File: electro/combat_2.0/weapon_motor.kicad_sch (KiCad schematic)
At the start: 16 parts, among them J4 Screw_Terminal_01x02, Q1 AO4402G, Q2 AO4402G, Q3 AO4402G, Q4 AO4402G, U4 LM2902, U5 ACS712xLCTR-20A

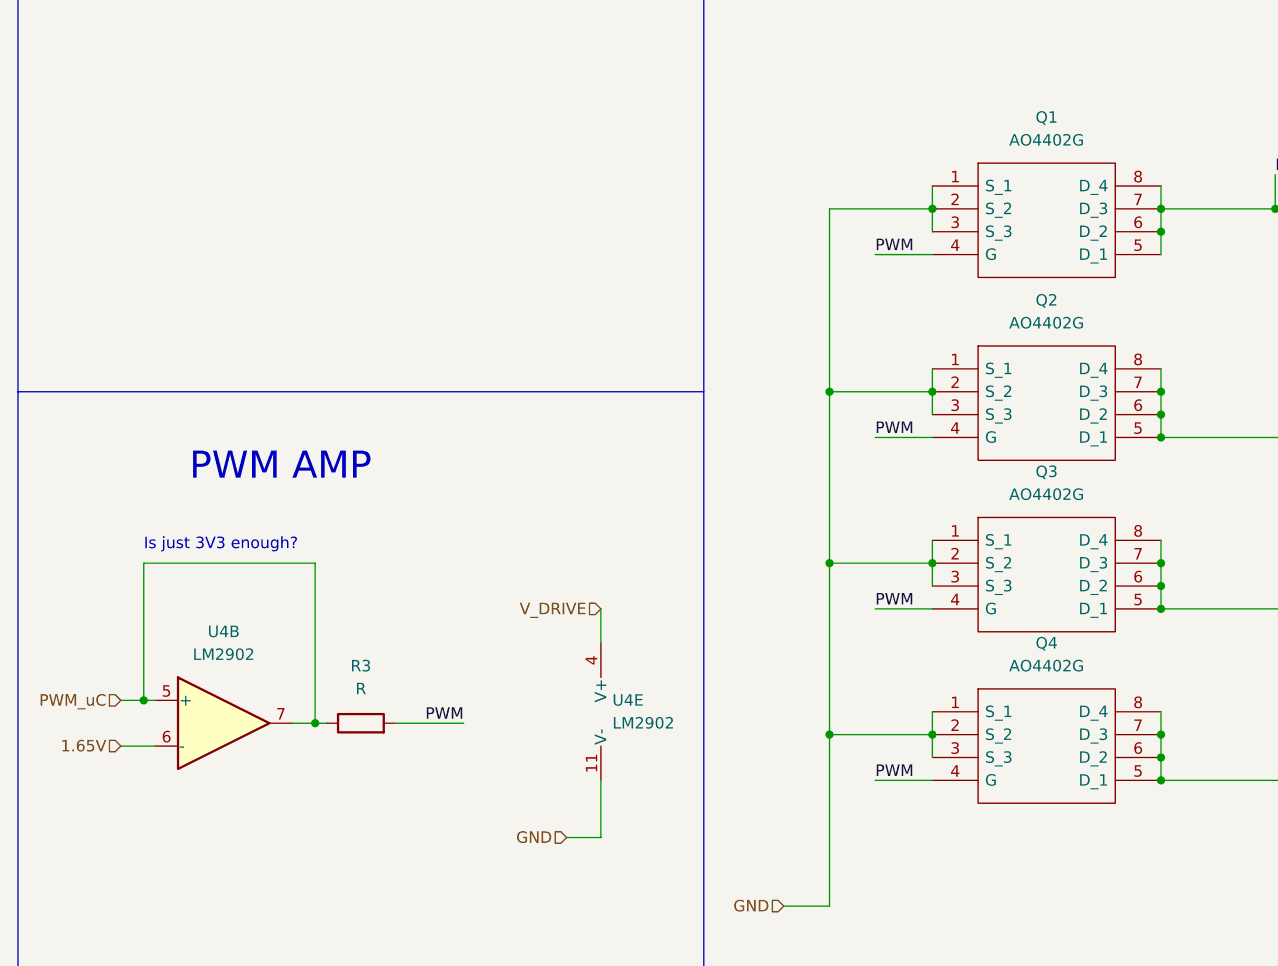
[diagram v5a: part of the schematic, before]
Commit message: Changed MCU to ESP32-DEVKITC, cleared some ERC errors
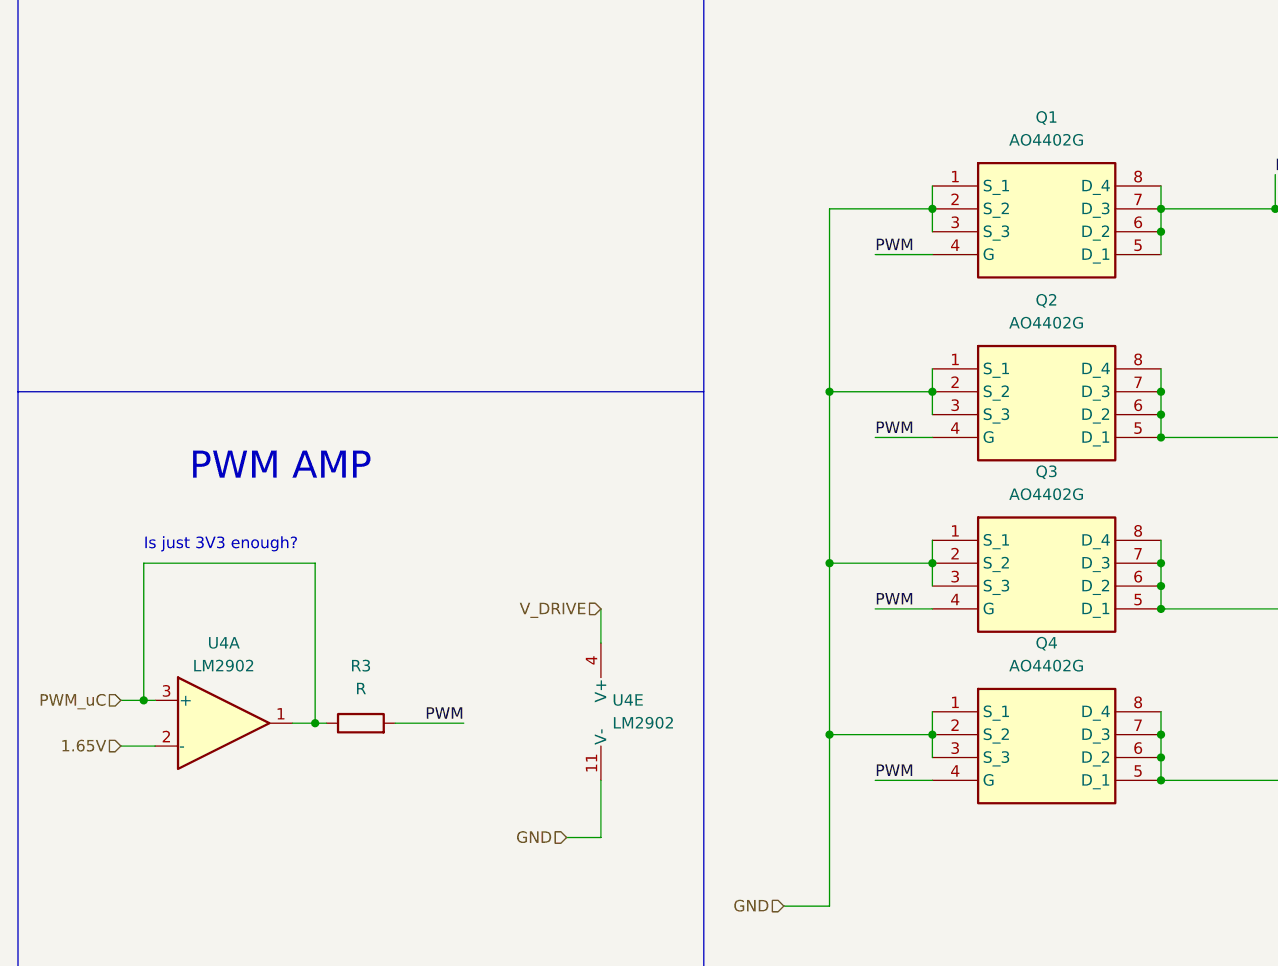
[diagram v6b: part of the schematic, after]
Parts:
- Q1, Q2, Q3, Q4: footprint MCS1802GS:SOIC127P600X175-8N -> (none)
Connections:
- net 1.65V: now also U4.2 (-); no longer U4.6 (-)
- net PWM_uC: now also U4.1, U4.3 (+); no longer U4.5 (+), U4.7
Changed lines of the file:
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@@
       (effects (font (size 1.27 1.27)))
     )
-    (property "Footprint" "MCS1802GS:SOIC127P600X175-8N" (at 148.59 116.84 0)
+    (property "Footprint" "" (at 148.59 116.84 0)
       (effects (font (size 1.27 1.27)) (justify left) hide)
     )
@@
       (effects (font (size 1.27 1.27)))
     )
-    (property "Footprint" "MCS1802GS:SOIC127P600X175-8N" (at 148.59 97.79 0)
+    (property "Footprint" "" (at 148.59 97.79 0)
       (effects (font (size 1.27 1.27)) (justify left) hide)
     )
@@
     )
   )
-  (symbol (lib_id "Amplifier_Operational:LM2902") (at 48.26 120.65 0) (unit 2)
-    (in_bom yes) (on_board yes) (dnp no) (fields_autoplaced)
-    (property "Reference" "U4" (at 48.26 110.49 0)
-      (effects (font (size 1.27 1.27)))
-    )
-    (property "Value" "LM2902" (at 48.26 113.03 0)
+  (symbol (lib_id "Amplifier_Operational:LM2902") (at 48.26 120.65 0) (unit 1)
+    (in_bom yes) (on_board yes) (dnp no) (fields_autoplaced)
+    (property "Reference" "U4" (at 48.26 111.76 0)
+      (effects (font (size 1.27 1.27)))
+    )
+    (property "Value" "LM2902" (at 48.26 114.3 0)
       (effects (font (size 1.27 1.27)))
     )
@@
       (project "combat_2.0"
         (path "/518cdd36-e3d2-496e-a534-90a14dea15b3/7634dbb1-8c54-4971-84cb-1ce817ae2ca8"
-          (reference "U4") (unit 2)
+          (reference "U4") (unit 1)
         )
       )
@@
       (effects (font (size 1.27 1.27)))
     )
-    (property "Footprint" "MCS1802GS:SOIC127P600X175-8N" (at 148.59 58.42 0)
+    (property "Footprint" "" (at 148.59 58.42 0)
       (effects (font (size 1.27 1.27)) (justify left) hide)
     )
@@
       (effects (font (size 1.27 1.27)))
     )
-    (property "Footprint" "MCS1802GS:SOIC127P600X175-8N" (at 148.59 78.74 0)
-      (effects (font (size 1.27 1.27)) (justify left) hide)
-    )
+    (property "Footprint" "" (at 148.59 78.74 0)
+      (effects (font (size 1.27 1.27)) (justify left) hide)
+    )

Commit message: Updated some footprints
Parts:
- C12: footprint (none) -> Capacitor_SMD:C_1206_3216Metric_Pad1.33x1.80mm_HandSolder
- C9: footprint Capacitor_SMD:C_0805_2012Metric -> Capacitor_SMD:C_1206_3216Metric_Pad1.33x1.80mm_HandSolder
- Q1, Q2, Q3, Q4: footprint (none) -> Package_SO:SOIC-8_3.9x4.9mm_P1.27mm
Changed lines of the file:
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@@
       (effects (font (size 1.27 1.27)))
     )
-    (property "Footprint" "" (at 148.59 116.84 0)
+    (property "Footprint" "Package_SO:SOIC-8_3.9x4.9mm_P1.27mm" (at 148.59 116.84 0)
       (effects (font (size 1.27 1.27)) (justify left) hide)
     )
@@
       (effects (font (size 1.27 1.27)))
     )
-    (property "Footprint" "" (at 148.59 97.79 0)
+    (property "Footprint" "Package_SO:SOIC-8_3.9x4.9mm_P1.27mm" (at 148.59 97.79 0)
       (effects (font (size 1.27 1.27)) (justify left) hide)
     )
@@
       (effects (font (size 1.27 1.27)) (justify left))
     )
-    (property "Footprint" "" (at 207.9752 127 0)
+    (property "Footprint" "Capacitor_SMD:C_1206_3216Metric_Pad1.33x1.80mm_HandSolder" (at 207.9752 127 0)
       (effects (font (size 1.27 1.27)) hide)
     )
@@
       (effects (font (size 1.27 1.27)) (justify left))
     )
-    (property "Footprint" "Capacitor_SMD:C_0805_2012Metric" (at 241.3 69.85 0)
+    (property "Footprint" "Capacitor_SMD:C_1206_3216Metric_Pad1.33x1.80mm_HandSolder" (at 241.3 69.85 0)
       (effects (font (size 1.27 1.27)) hide)
     )
@@
       (effects (font (size 1.27 1.27)))
     )
-    (property "Footprint" "" (at 148.59 58.42 0)
+    (property "Footprint" "Package_SO:SOIC-8_3.9x4.9mm_P1.27mm" (at 148.59 58.42 0)
       (effects (font (size 1.27 1.27)) (justify left) hide)
     )
@@
       (effects (font (size 1.27 1.27)))
     )
-    (property "Footprint" "" (at 148.59 78.74 0)
-      (effects (font (size 1.27 1.27)) (justify left) hide)
-    )
+    (property "Footprint" "Package_SO:SOIC-8_3.9x4.9mm_P1.27mm" (at 148.59 78.74 0)
+      (effects (font (size 1.27 1.27)) (justify left) hide)
+    )

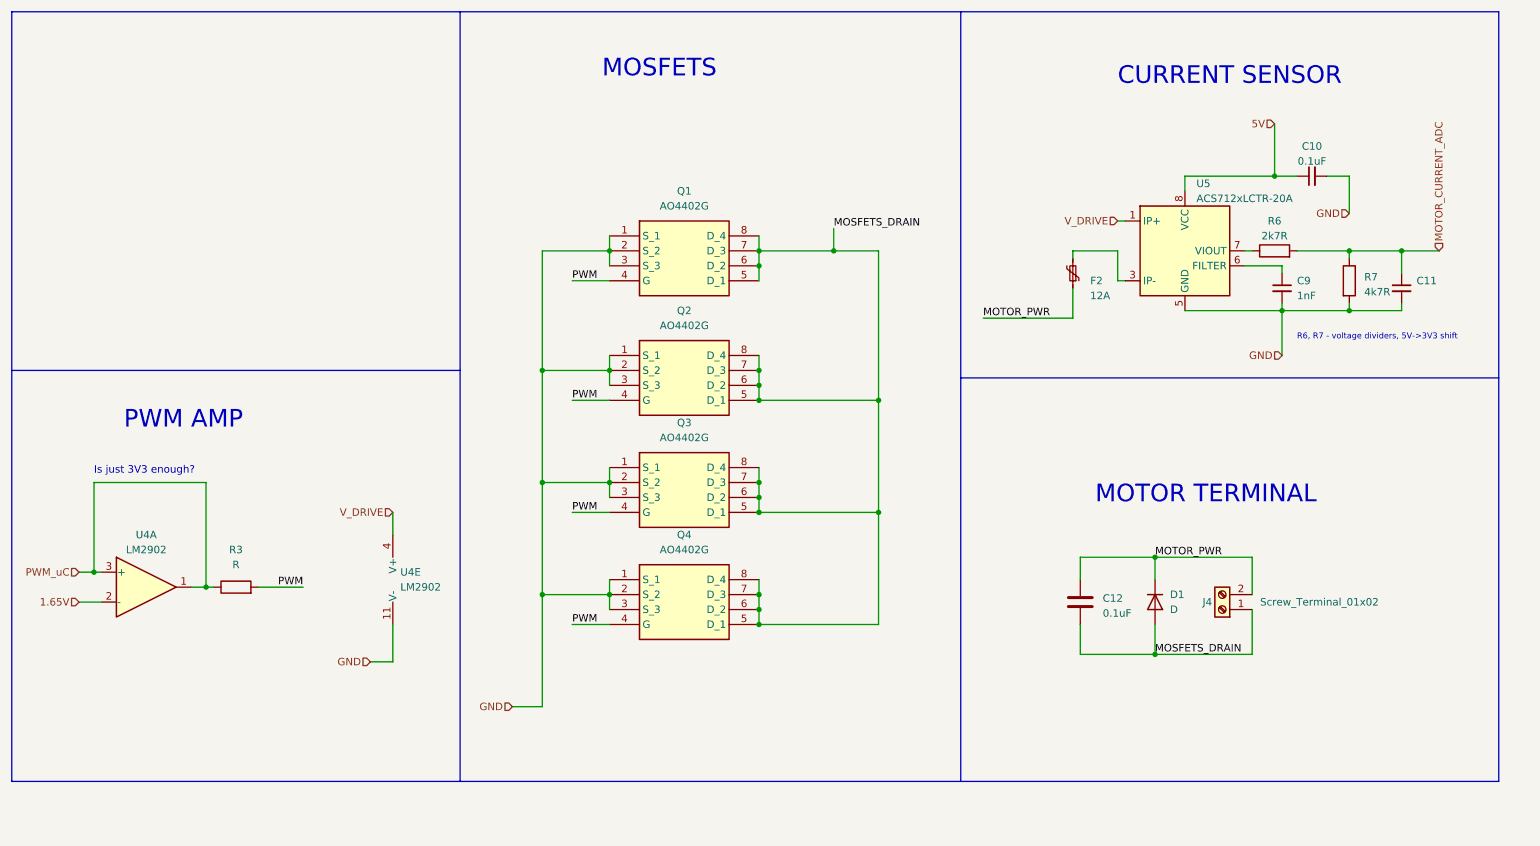
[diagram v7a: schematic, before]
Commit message: Changed Devkit for ESP32-WROOM device. Added LDO, some other peripherals
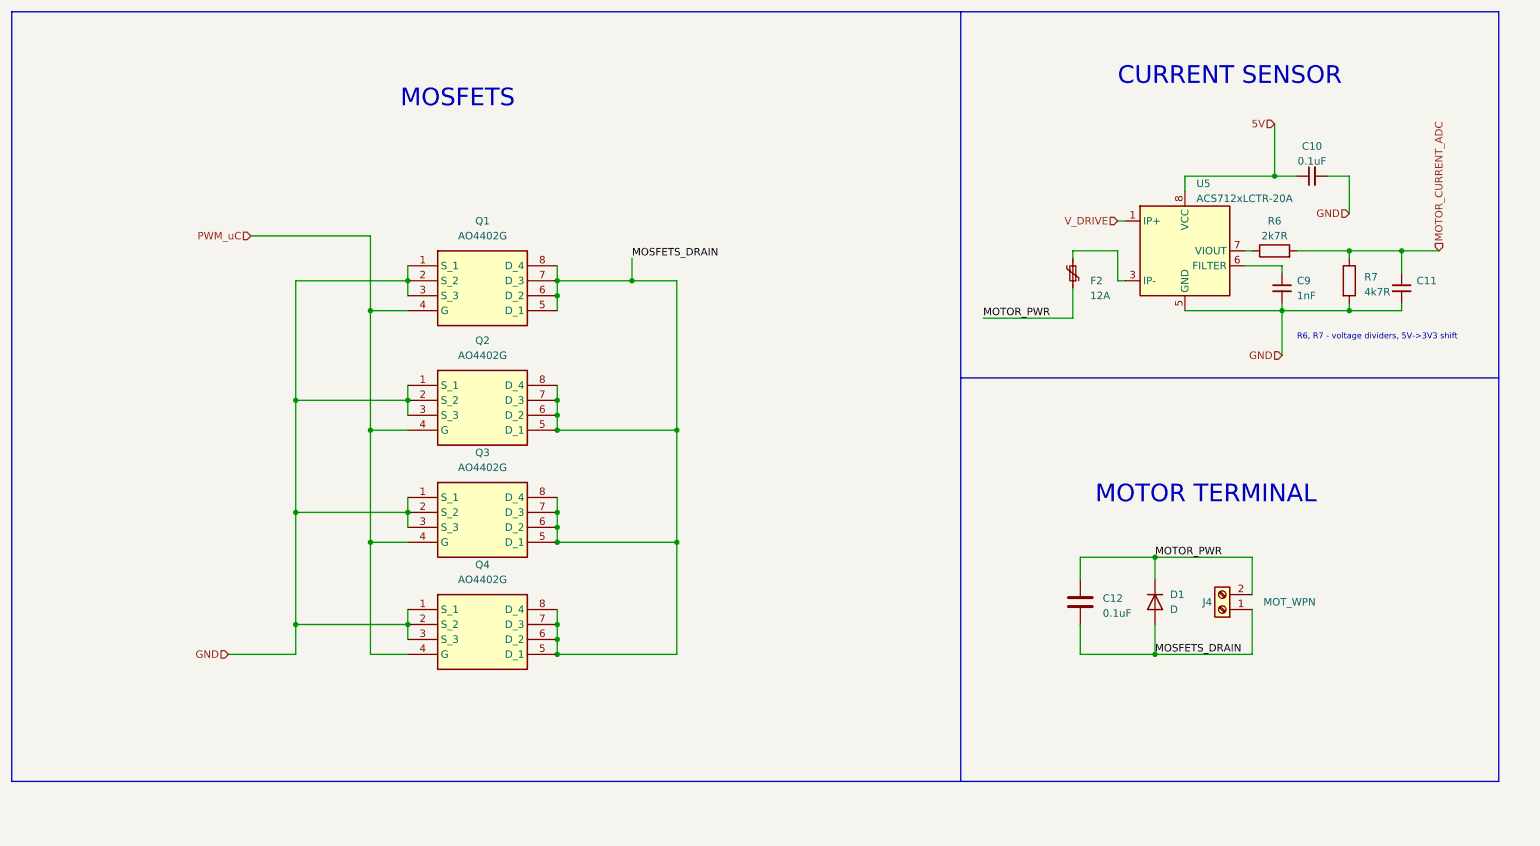
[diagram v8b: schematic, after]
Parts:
- removed R3: R, Resistor_SMD:R_1206_3216Metric_Pad1.30x1.75mm_HandSolder, symbol Device:R
- removed U4: LM2902, Package_SO:SOIC-14_3.9x8.7mm_P1.27mm, symbol Amplifier_Operational:LM2902
- J4: value Screw_Terminal_01x02 -> MOT_WPN
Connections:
- net PWM is gone; now on net PWM_uC: Q1.4 (G), Q2.4 (G), Q3.4 (G), Q4.4 (G)
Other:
- note removed: "Is just 3V3 enough?"
- note removed: "PWM AMP"
- moved on the sheet: Q1, Q2, Q3, Q4
